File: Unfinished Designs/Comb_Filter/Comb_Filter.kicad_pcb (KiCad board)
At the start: 2 copper layers, 100 x 110 mm, 164 parts, among them J1 AudioJack1_Switch, J10 AudioJack1_Switch, J11 AudioJack1_Switch, J12 AudioJack1_Switch, J13 AudioJack1_Switch, J2 Conn_02x05_Odd_Even, J3 AudioJack1_Switch, J4 AudioJack1_Switch, J5 AudioJack1_Switch, J6 AudioJack1_Switch, J7 AudioJack1_Switch, J8 AudioJack1_Switch, J9 AudioJack1_Switch, U1 TL074, U2 TL074, U3 TL074, U4 TL074

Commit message: 1-29-2021 Comb
Started Layout of Comb Filter
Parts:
- added J14: Conn_01x07, Pin_Headers:Pin_Header_Straight_1x07_Pitch2.54mm, F.Cu at (20.0, 50.0)
- added J15: Conn_01x07, Pin_Headers:Pin_Header_Straight_1x07_Pitch2.54mm, F.Cu at (16.0, 50.0)
- added J16: Conn_01x07, Pin_Headers:Pin_Header_Straight_1x07_Pitch2.54mm, F.Cu at (80.0, 50.0)
- added J17: Conn_01x07, Pin_Headers:Pin_Header_Straight_1x07_Pitch2.54mm, F.Cu at (84.0, 50.0)
- C1, C10, C11, C12, C13, C14, C15, C16, C17, C18, C19, C2, C20, C21, C22, C23, C24, C25, C26, C27, C28, C29, C3, C30, C31, C32, C33, C34, C35, C36, C37, C38, C39, C4, C40, C41, C42, C43, C44, C5, C6, C7, C8, C9, J2, R1, R10, R11, R12, R13, R14, R15, R16, R17, R18, R19, R2, R20, R21, R22, R23, R24, R25, R26, R27, R28, R29, R3, R30, R31, R32, R33, R34, R35, R36, R37, R38, R39, R4, R40, R41, R42, R43, R44, R45, R46, R47, R48, R49, R5, R50, R51, R52, R53, R54, R55, R56, R57, R58, R59, R6, R60, R61, R62, R63, R64, R65, R66, R67, R68, R69, R7, R70, R71, R72, R73, R74, R75, R76, R77, R8, R9, RV1, RV10, RV11, RV12, RV13, RV14, RV15, RV16, RV2, RV3, RV4, RV5, RV6, RV7, RV8, RV9, U1, U2, U3, U4: moved to B.Cu
- moved C13 408.6 mm to (103.9, 294.6)
- moved C3 408.6 mm to (88.8, 294.6)
- moved R15 408.6 mm to (96.4, 294.6)
- moved RV11 406.7 mm to (111.0, 293.5)
- moved C27 401.2 mm to (88.8, 290.5)
- moved R1 401.2 mm to (96.4, 290.5)
- moved R22 401.2 mm to (103.9, 290.5)
- moved RV1 395.6 mm to (111.0, 287.4)
- moved R19 393.8 mm to (96.4, 286.4)
- moved R4 393.8 mm to (88.8, 286.4)
- moved R42 393.8 mm to (103.9, 286.4)
- moved R30 386.5 mm to (94.0, 282.3)
- moved R52 386.5 mm to (101.5, 282.3)
- moved R66 386.5 mm to (109.1, 282.3)
- moved C14 385.7 mm to (86.4, 281.9)
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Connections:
- net Net-(FADE1-Pad2) renamed <100_Out
- net Net-(FADE10-Pad2) renamed >7k_Out
- net Net-(FADE2-Pad2) renamed 200_Out
- net Net-(FADE3-Pad2) renamed 350_Out
- net Net-(FADE4-Pad2) renamed 500_Out
- net Net-(FADE5-Pad2) renamed 700_Out
- net Net-(FADE6-Pad2) renamed 1k_Out
- net Net-(FADE7-Pad2) renamed 1k4_Out
- net Net-(FADE8-Pad2) renamed 2k_Out
- net Net-(FADE9-Pad2) renamed 3k5_Out
- C1 pad 2: Net-(C1-Pad2) -> Input
- J1 pad 1: GND -> Net-(J1-Pad1)
- J1 pad 2: GND -> Net-(J1-Pad1)
- J1 pad 3: Net-(C1-Pad2) -> Net-(J1-Pad3)
- J10 pad 1: GND -> Net-(J10-Pad1)
- J10 pad 3: 2k -> Net-(J10-Pad3)
- J11 pad 1: GND -> Net-(J1-Pad1)
- J11 pad 3: 3k5 -> Net-(J11-Pad3)
- J12 pad 1: GND -> Net-(J10-Pad1)
- J12 pad 3: >7k -> Net-(J12-Pad3)
- J13 pad 1: GND -> Net-(J10-Pad1)
- J3 pad 1: GND -> Net-(J1-Pad1)
- J3 pad 3: <100 -> Net-(J15-Pad1)
- J4 pad 1: GND -> Net-(J10-Pad1)
- J4 pad 3: 200 -> Net-(J17-Pad1)
- J5 pad 1: GND -> Net-(J1-Pad1)
- J5 pad 3: 350 -> Net-(J15-Pad2)
- J6 pad 1: GND -> Net-(J10-Pad1)
- J6 pad 3: 500 -> Net-(J17-Pad2)
- J7 pad 1: GND -> Net-(J1-Pad1)
- J7 pad 3: 700 -> Net-(J15-Pad3)
- J8 pad 1: GND -> Net-(J10-Pad1)
- J8 pad 3: 1k -> Net-(J17-Pad3)
- J9 pad 1: GND -> Net-(J1-Pad1)
- J9 pad 3: 1k4 -> Net-(J15-Pad4)
- R64 pad 1: Net-(J13-Pad3) -> Output
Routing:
- net Net-(J17-Pad1): track 0.00 -> 52.9 mm
- net Net-(J1-Pad3): track 0.00 -> 52.2 mm
- net Net-(J15-Pad1): track 0.00 -> 46.5 mm
- net Net-(J13-Pad3): track 0.00 -> 43.2 mm
- net Net-(J17-Pad2): track 0.00 -> 35.4 mm
- net Net-(J11-Pad3): track 0.00 -> 34.7 mm
- net Net-(J15-Pad2): track 0.00 -> 28.7 mm
- net Net-(J12-Pad3): track 0.00 -> 27.0 mm
- net Net-(J15-Pad4): track 0.00 -> 18.9 mm
- net Net-(J17-Pad3): track 0.00 -> 18.0 mm
- net Net-(J15-Pad3): track 0.00 -> 12.5 mm
- net Net-(J10-Pad3): track 0.00 -> 12.2 mm
- added copper zone on B.Cu, net Net-(J1-Pad1)
- added copper zone on F.Cu, net Net-(J1-Pad1)
- added copper zone on B.Cu, net Net-(J10-Pad1)
- added copper zone on F.Cu, net Net-(J10-Pad1)

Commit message: Update Summary
Updated the Overall Desdign File
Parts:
- moved U1 245.9 mm to (74.2, 22.2)
- moved R14 216.3 mm to (71.0, 4.75)
- moved U3 214.2 mm to (26.0, 21.2)
- moved U2 160.8 mm to (25.7, 93.2)
- moved C1 153.7 mm to (23.5, 64.7), turned to 90 degrees
- moved U4 153.7 mm to (74.5, 88.5)
- moved C39 121.0 mm to (40.0, 105.5), turned to 90 degrees
- moved C44 120.5 mm to (60.0, 105.5), turned to 270 degrees
- moved C41 12.6 mm to (9.90, 209.1), turned to 90 degrees

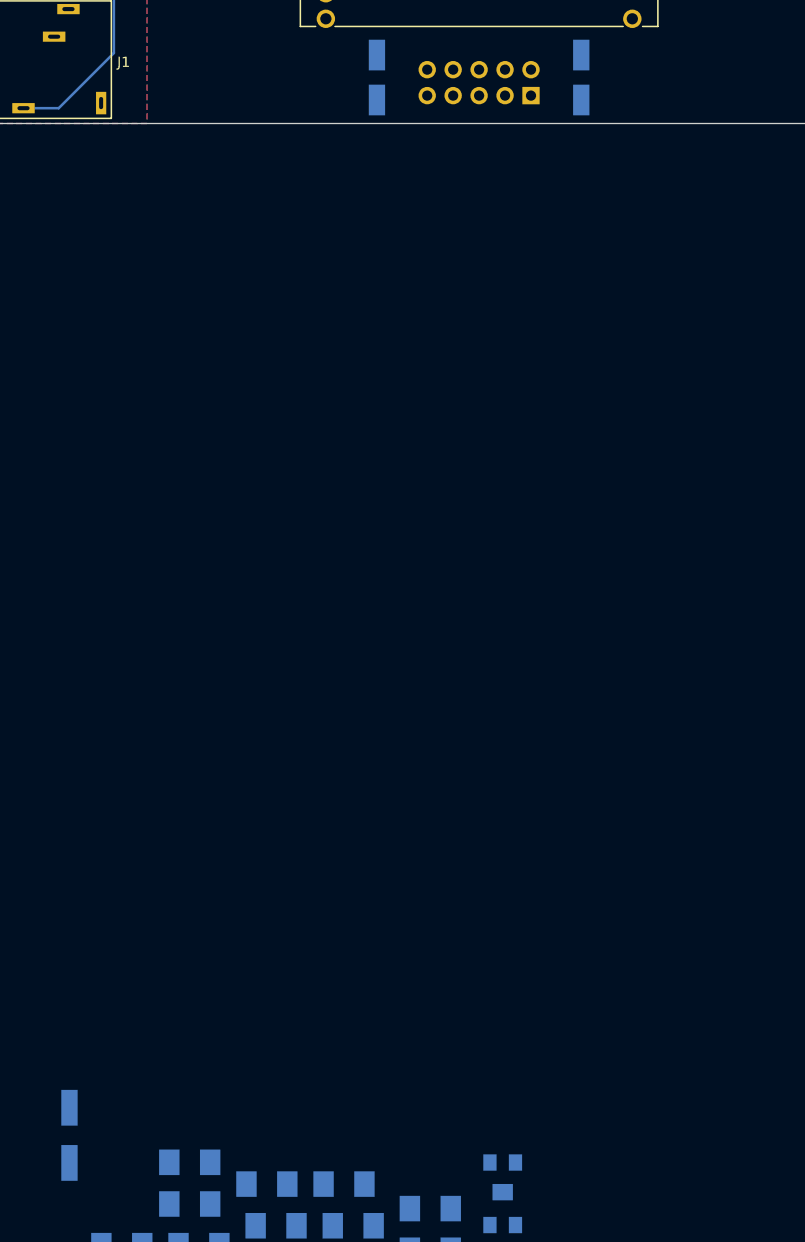
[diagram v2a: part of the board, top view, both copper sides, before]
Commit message: KiCAD 6.0 Update
Updated all the project files to Version 6.0 of KiCAD.  No change to Gerbers or Schematics.
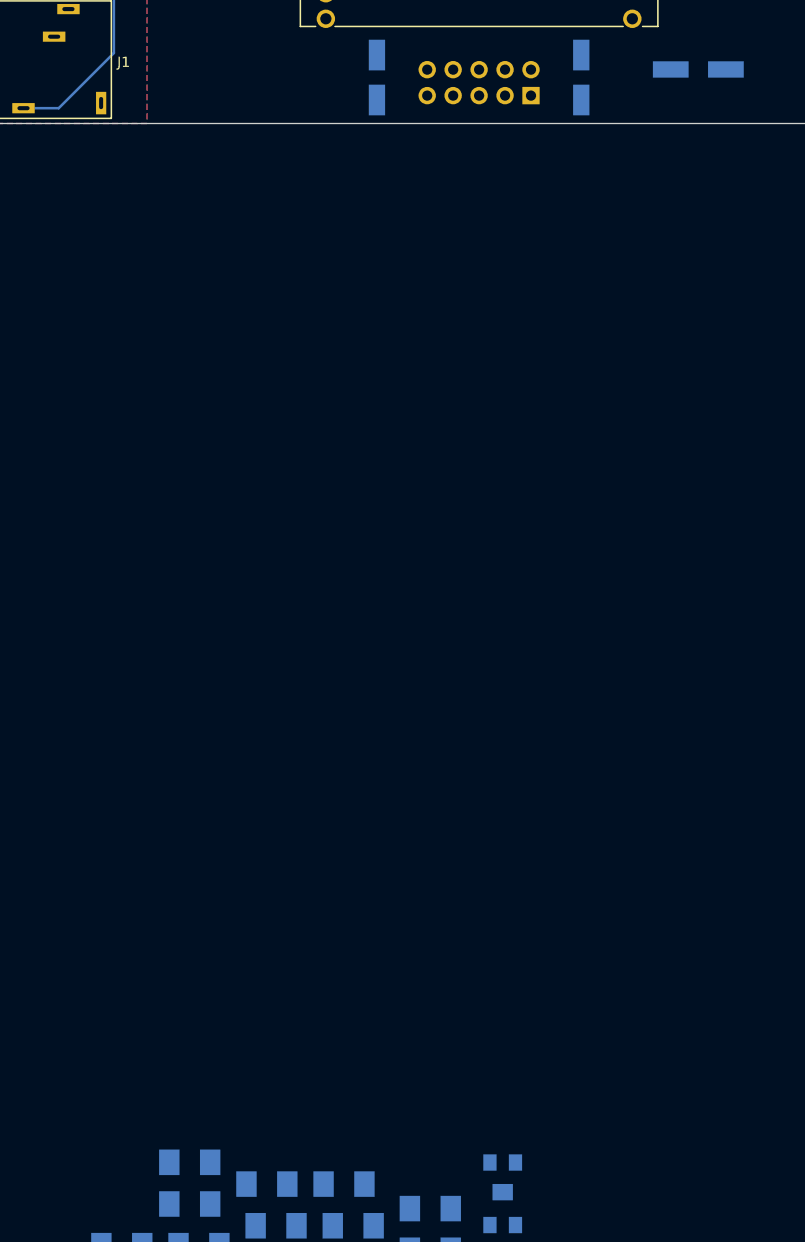
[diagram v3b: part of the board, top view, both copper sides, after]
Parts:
- moved C41 121.1 mm to (71.5, 104.7), turned to 180 degrees
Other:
- net class Default removed
- net class PWR removed

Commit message: Comb Placements
started placing components on Comb Filter
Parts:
- moved C42 257.3 mm to (25.9, 12.8)
- moved C40 236.3 mm to (74.2, 12.2)
- moved C43 161.4 mm to (74.4, 80.3)
- moved C41 49.7 mm to (25.9, 84.8), turned to 0 degrees
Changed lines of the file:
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@@
   )
   (footprint "Capacitors_SMD:CP_Elec_6.3x5.8" (layer "B.Cu")
-    (at 42.725001 246.459999)
+    (at 74.168 12.2428)
     (descr "SMT capacitor, aluminium electrolytic, 6.3x5.8")
     (attr smd)
@@
   )
   (footprint "Capacitors_SMD:CP_Elec_6.3x5.8" (layer "B.Cu")
-    (at 71.46 104.71 180)
+    (at 25.908 84.836)
     (descr "SMT capacitor, aluminium electrolytic, 6.3x5.8")
     (attr smd)
@@
     (fp_line (start -2.48 -3.15) (end 3.15 -3.15) (layer "B.Fab") (width 0.1))
     (fp_circle (center 0 0) (end 0.5 -3) (layer "B.Fab") (width 0.1) (fill none))
-    (pad "1" smd rect locked (at -2.7 0) (size 3.5 1.6) (layers "B.Cu" "B.Paste" "B.Mask")
+    (pad "1" smd rect locked (at -2.7 0 180) (size 3.5 1.6) (layers "B.Cu" "B.Paste" "B.Mask")
       (net 54 "+12"))
-    (pad "2" smd rect locked (at 2.7 0) (size 3.5 1.6) (layers "B.Cu" "B.Paste" "B.Mask")
+    (pad "2" smd rect locked (at 2.7 0 180) (size 3.5 1.6) (layers "B.Cu" "B.Paste" "B.Mask")
       (net 55 "-12"))
     (model "Capacitors_SMD.3dshapes/CP_Elec_6.3x5.8.wrl"
@@
   )
   (footprint "Capacitors_SMD:CP_Elec_6.3x5.8" (layer "B.Cu")
-    (at 73.475001 265.589999)
+    (at 25.8572 12.7508)
     (descr "SMT capacitor, aluminium electrolytic, 6.3x5.8")
     (attr smd)
@@
   )
   (footprint "Capacitors_SMD:CP_Elec_6.3x5.8" (layer "B.Cu")
-    (at 26.125001 234.279999)
+    (at 74.422 80.3148)
     (descr "SMT capacitor, aluminium electrolytic, 6.3x5.8")
     (attr smd)
